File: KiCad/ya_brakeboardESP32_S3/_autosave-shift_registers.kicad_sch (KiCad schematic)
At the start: 10 parts, among them J1 Screw_Terminal_01x04, J2 SR_0_Terminal, J3 SR_1_Terminal, J4 SR_2_Terminal, U1 TPIC6B595N, U2 TPIC6B595N, U3 TPIC6B595N

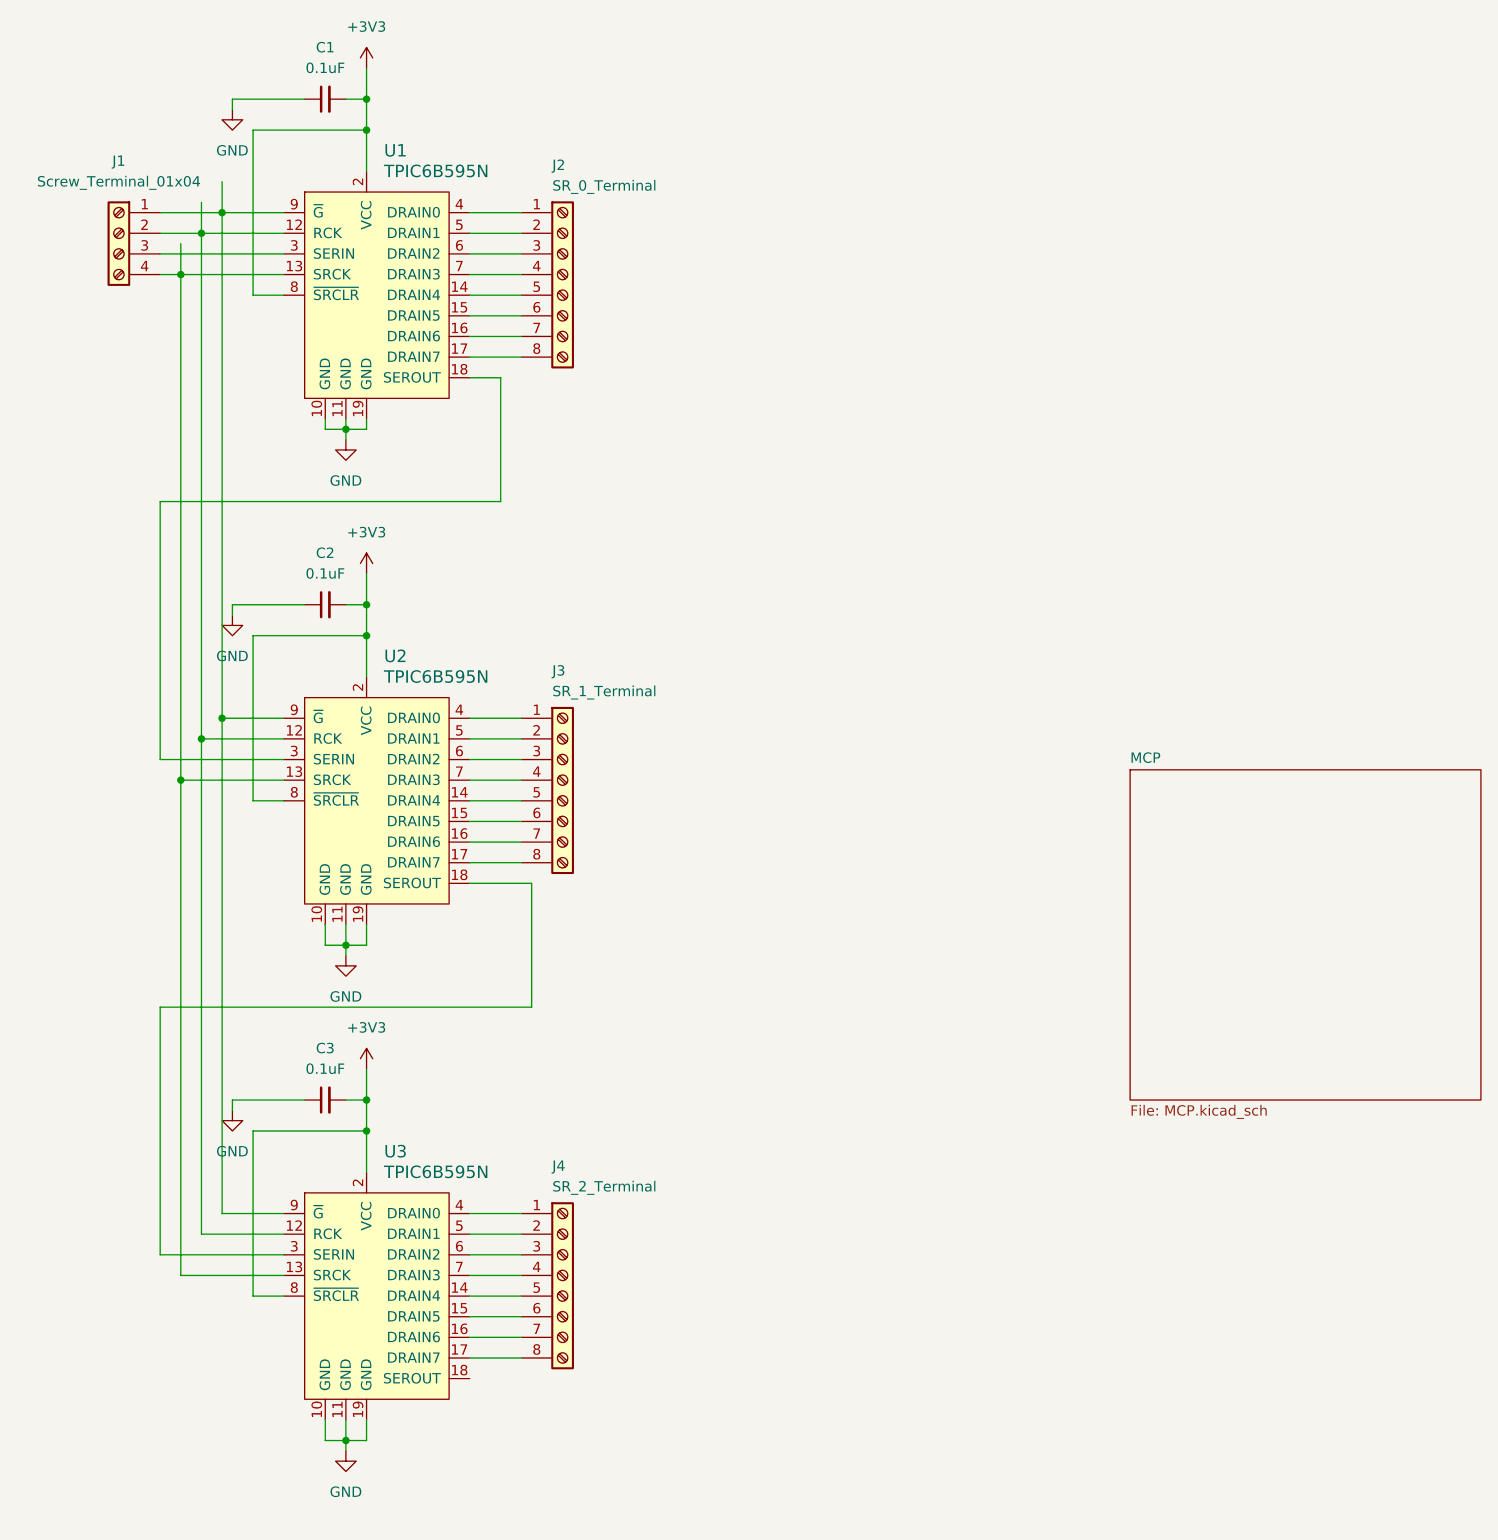
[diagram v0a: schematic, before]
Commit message: alarm clear outputs on expanders. want to move them to SRs
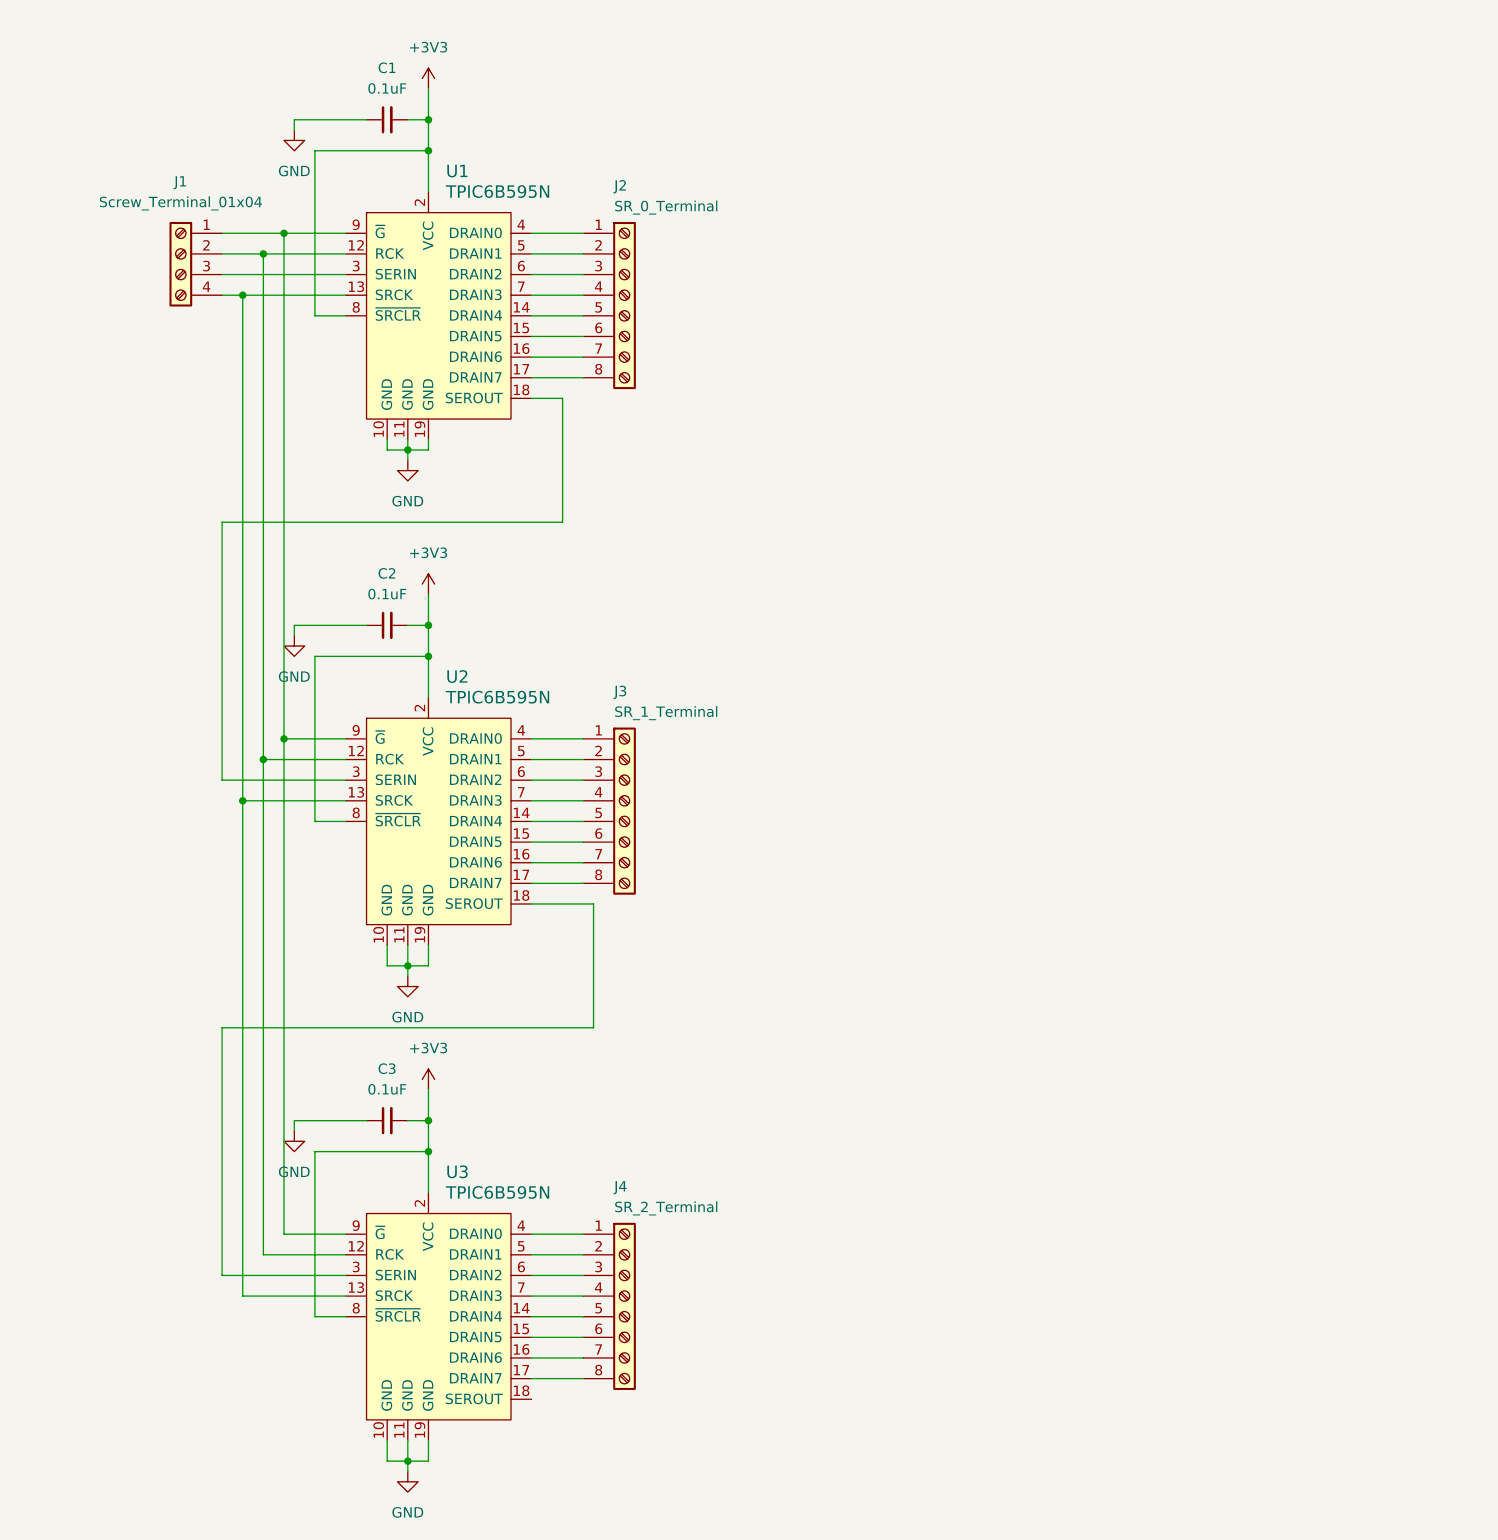
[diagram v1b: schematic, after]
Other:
- removed sheet MCP
- moved on the sheet: C1, C2, C3, J1, J2, J3, J4, U1, U2, U3
